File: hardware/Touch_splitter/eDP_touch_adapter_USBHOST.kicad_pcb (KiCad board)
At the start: 2 copper layers, 26 x 26.1 mm, 32 parts, among them J1 Conn_01x40, J3 Conn_01x40, J4 USB_B_Micro, U1 RP2354_60QFN, Y1 12MHz

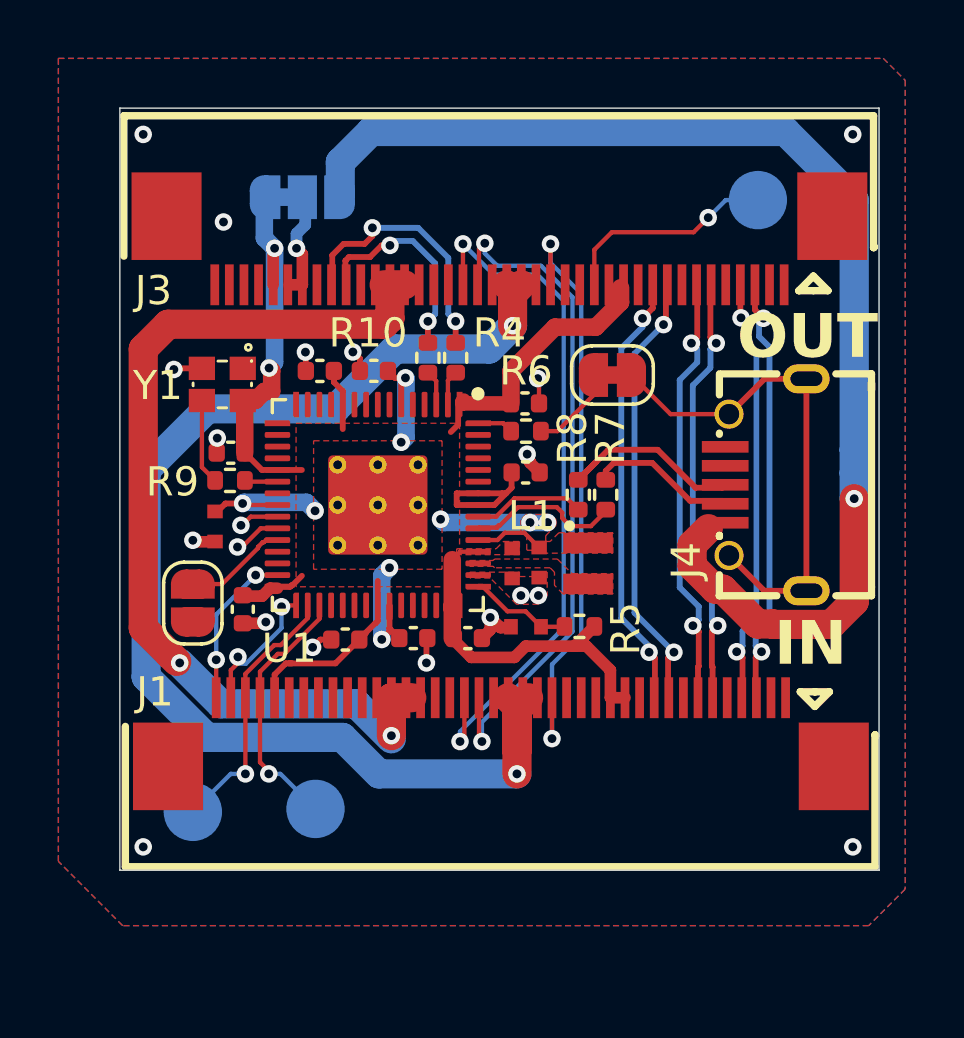
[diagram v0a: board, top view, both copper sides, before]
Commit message: add USB host to I2C board based on RP2354 MCU
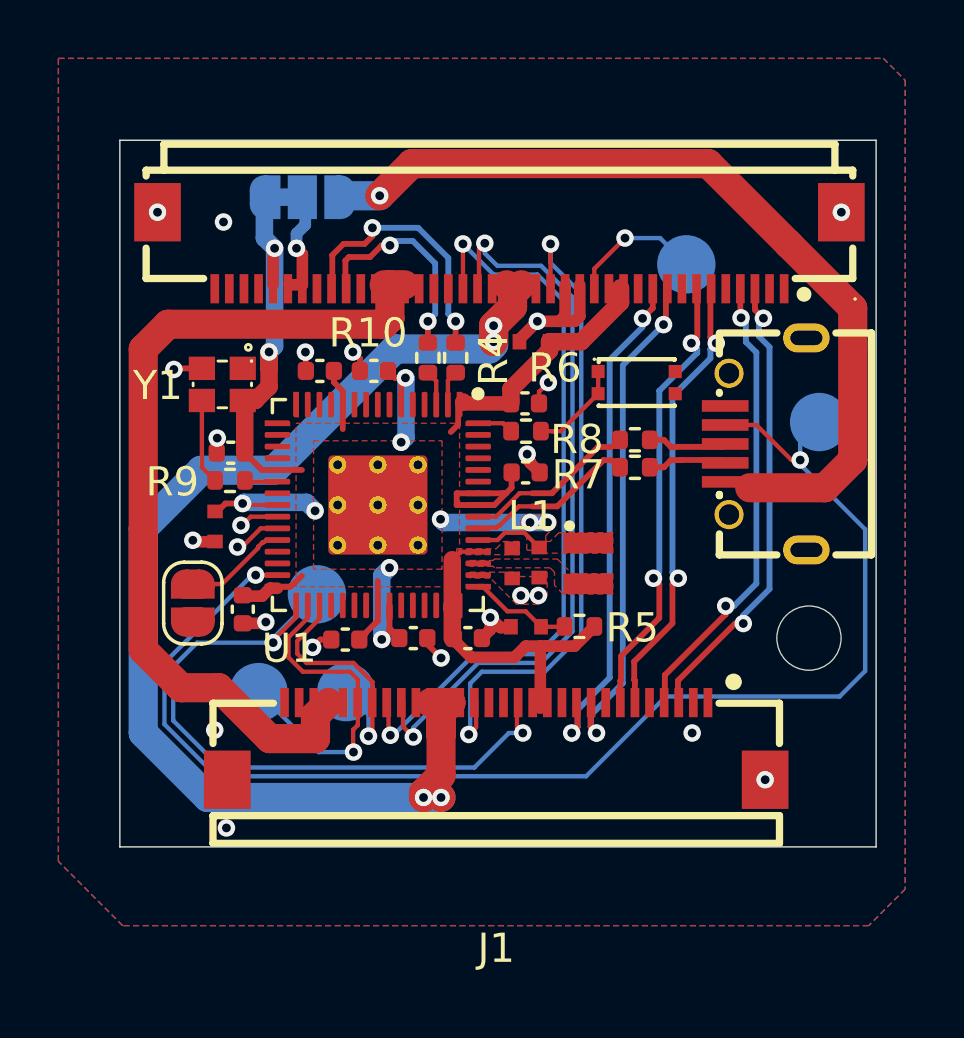
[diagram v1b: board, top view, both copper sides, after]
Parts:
- removed JP3: BOOT, Jumper:SolderJumper-2_P1.3mm_Bridged_RoundedPad1.0x1.5mm
- added C1: 4.7u 10V, RP2350_60QFN_minimal:C_0402_1005Metric_small_pads, F.Cu at (122.5, 105.5)
- added H1: MountingHole, MountingHole:MountingHole_2.2mm_M2, F.Cu at (131.9, 115.6)
- added SW1: SW_Push, easyeda2kicad:SW-SMD_4P-L2.5-W1.6-LS2.9_STI-055A12AX, F.Cu at (126.0, 106.9)
- added TP4: TestPoint_Small, TestPoint:TestPoint_Pad_D2.0mm, B.Cu at (115.0, 114.1)
- added TP5: TestPoint_Small, TestPoint:TestPoint_Pad_D2.0mm, B.Cu at (132.2, 108.2)
- J1: value Conn_01x40 -> Conn_01x30; footprint Library:FPC-SMD_40P-P0.50_L4.4-W25.6 -> easyeda2kicad:FPC-SMD_30P-P0.50_FPC-0.5FX-30PWBH15
- J3: footprint Library:FPC-SMD_40P-P0.50_L4.4-W25.6 -> easyeda2kicad:FPC-SMD_XUNPU_FPC-0.5FX-40PWBH15
- moved TP2 4.68 mm to (113.0, 117.5)
- moved TP3 4.14 mm to (116.0, 117.5)
- moved TP1 3.29 mm to (127.7, 102.8)
- moved R8 2.70 mm to (125.9, 108.8), turned to 180 degrees
- moved J4 1.40 mm to (130.4, 109.0)
- moved R7 1.37 mm to (125.9, 109.8), turned to 180 degrees
- moved J1 0.35 mm to (121.2, 119.2)
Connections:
- net Net-(U1-USB_DM) renamed /MCU_USB_DN
- net Net-(U1-USB_DP) renamed /MCU_USB_DP
- J1 pad 14: unconnected-(J1-Pin_14-Pad14) -> /GPIO19
- J1 pad 24: unconnected-(J1-Pin_24-Pad24) -> /GPIO21
- J1 pad 25: unconnected-(J1-Pin_25-Pad25) -> /GPIO20
- J4 pad 4: unconnected-(J4-ID-Pad4) -> /GPIO18
- J4 pad 6: Net-(J4-Shield) -> GND
- R6 pad 2: /~{USB_BOOT} -> /~{BOOT}
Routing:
- net /GPIO18: track 5.61 -> 46.2 mm
- net /GPIO19: track 4.65 -> 23.8 mm
- net Net-(J4-Shield): track 17.7 -> 0.00 mm
- net VBUS: track 42.2 -> 29.2 mm
- net GND: track 9.51 -> 15.6 mm, vias 18 -> 21
- net +3V3: track 50.8 -> 45.4 mm
- net /UDP: track 6.89 -> 2.73 mm
- net /~{BOOT}: track 0.00 -> 3.44 mm
- net /~{USB_BOOT}: track 3.00 -> 0.00 mm
- net /TEST: track 7.50 -> 4.51 mm
- net /AUX_N: track 15.3 -> 18.0 mm
- net /AUX_P: track 15.5 -> 18.2 mm
- net /BL_PWR: track 32.2 -> 29.6 mm, vias 2 -> 0
- net /UDN: track 5.09 -> 2.73 mm
- net /GPIO20: track 9.12 -> 11.4 mm
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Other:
- board size 26 x 26.1 mm -> 25.9 x 24.2 mm
- board text added: "NOTE: select correct impedance (coplanar) for differential tracks"
- board text removed: "IN"
- board text removed: "OUT"

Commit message: review and update manufacturing constraints (via size, etc.)
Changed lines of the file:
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@@
 			(at 0 7.093 0)
 			(layer "F.SilkS")
+			(hide yes)
 			(effects
 				(font
